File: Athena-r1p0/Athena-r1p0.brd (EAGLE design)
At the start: 33 x 55.1 mm, 81 parts, among them J1 MF-CON-MICROUSB-RIGHT, J2 G800LS588010THR, J3 TC2030-IDC-NL, J4 MF-CON-2.54mm-01x08, J5 MF-CON-2.54mm-01x08, J6 MF-CON-2.54mm-01x07, SW1 MF-SW-TACT-6MM, SW2 MF-SW-TACT-6MM, U1 PRTR5V0U2X,215, U2 MCP73831/2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

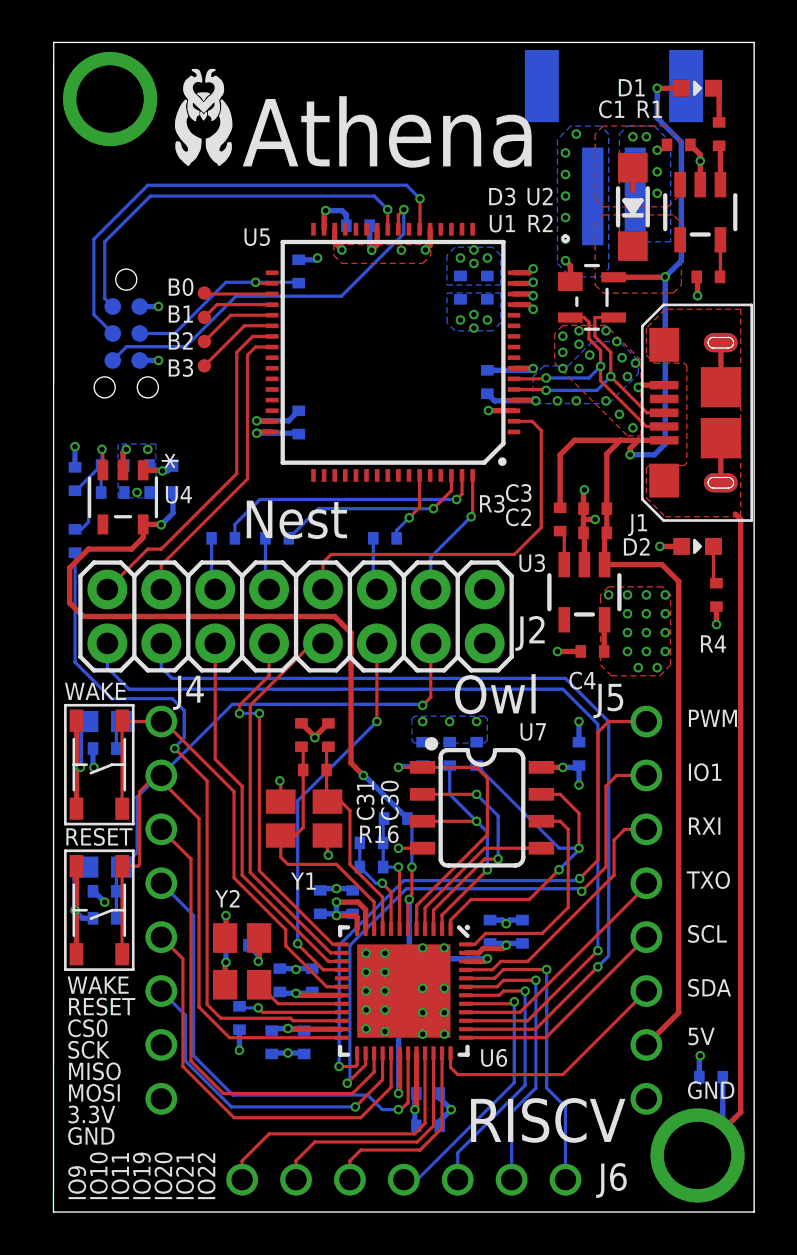
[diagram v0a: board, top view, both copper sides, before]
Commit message: Updated design
Removed off-board debug header
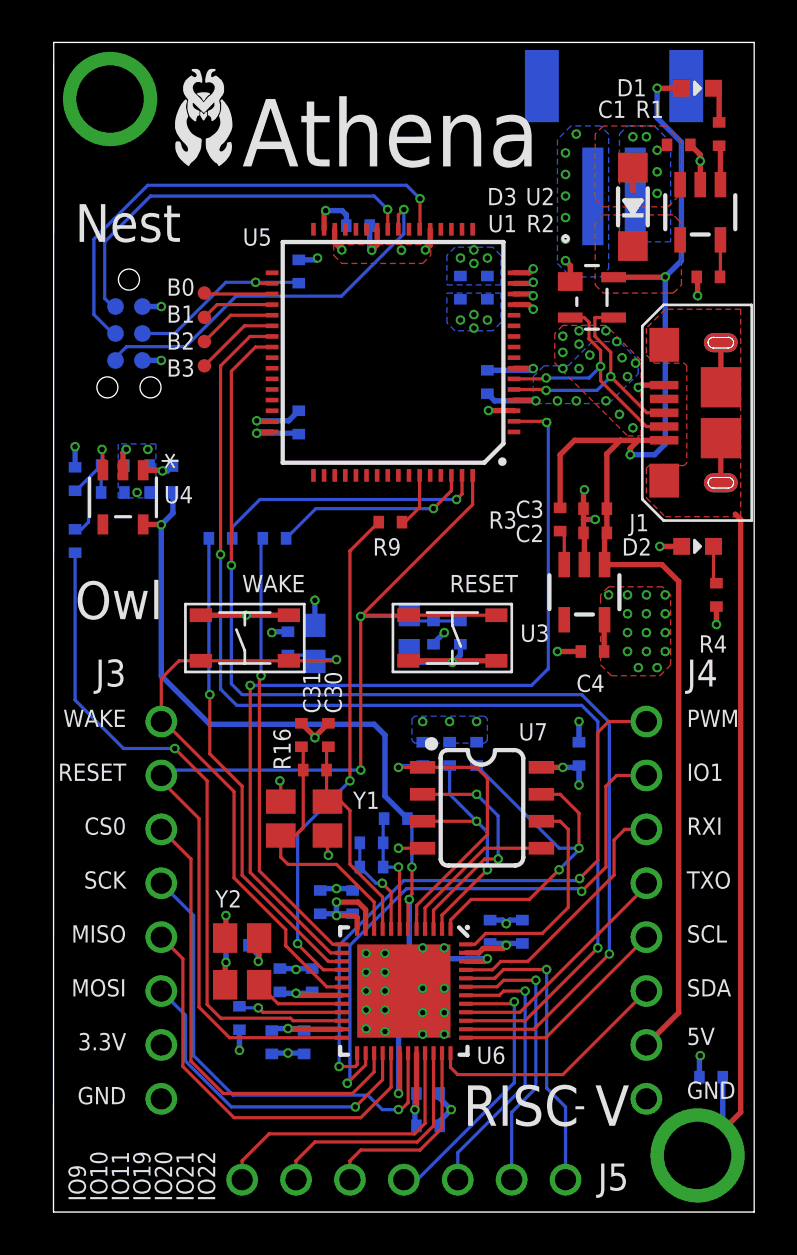
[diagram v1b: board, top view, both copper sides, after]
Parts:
- removed J6: MF-CON-2.54mm-01x07, Athena-r1p0:PTH_2.54MM_01X07
- J2: value G800LS588010THR -> TC2030-IDC-NL; device Athena-r1p0:2X8 -> Athena-r1p0:TAG_TC2030-IDC-NL
- J3: value TC2030-IDC-NL -> MF-CON-2.54mm-01x08; device Athena-r1p0:TAG_TC2030-IDC-NL -> Athena-r1p0:PTH_2.54MM_01X08
- J5: value MF-CON-2.54mm-01x08 -> MF-CON-2.54mm-01x07; device Athena-r1p0:PTH_2.54MM_01X08 -> Athena-r1p0:PTH_2.54MM_01X07
- moved J3 27.2 mm to (5.08, 14.2), flipped to the top
- moved J4 22.9 mm to (27.9, 14.2)
- moved C28 21.5 mm to (19.2, 27.3), turned to 270 degrees
- moved SW2 21.0 mm to (18.8, 27.1), turned to 180 degrees
- moved R14 19.7 mm to (17.9, 27.3), turned to 90 degrees
- moved D5 18.1 mm to (16.8, 27.3), turned to 90 degrees
- moved J5 17.1 mm to (16.5, 1.52), turned to 0 degrees
- moved J2 14.6 mm to (3.56, 41.4), flipped to the bottom, turned to 270 degrees
- moved D4 10.6 mm to (12.3, 26.8), turned to 270 degrees
- moved R13 9.96 mm to (11.0, 26.8), turned to 270 degrees
- moved SW1 9.09 mm to (9.02, 27.1), turned to 0 degrees
- moved R9 0.80 mm to (15.9, 32.5), flipped to the top, turned to 180 degrees
- moved R10 0.13 mm to (10.4, 31.8)
- moved R11 0.13 mm to (7.87, 31.8)
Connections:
- removed net JTAG_TCK_NEST: J2.8, R10.P$2
- removed net JTAG_TDI_NEST: J2.12, R9.P$2
- removed net JTAG_TDO_NEST: J2.10, U5.2
- removed net JTAG_TMS_NEST: J2.6, R11.P$1
- removed net RESET_NEST: J2.14, U5.64
- removed net UART_RX: J2.3, U6.38
- removed net UART_RX_NEST: J2.2, U5.39
- removed net UART_TX: J2.1, U6.39
- removed net UART_TX_NEST: J2.4, U5.40
- new net UART_RX_MK22: U5.39, U6.39
- new net UART_TX_MK22: U5.40, U6.38
- net 3.3V: now also J2.1, J3.P$7; no longer J3.1, J4.P$7
- net CS0: now also J3.P$3; no longer J4.P$3
- net DBG_RESET: now also J2.3; no longer J3.3
- net DBG_SWDCLK: now also J2.4; no longer J3.4
- net DBG_SWDIO: now also J2.2; no longer J3.2
- net DBG_SWO: now also J2.6; no longer J3.6
- net GND: now also J2.5, J3.P$8, MGT2.P$1; no longer J2.15, J2.16, J3.5, J5.P$8
- net IO1: now also J4.P$2; no longer J5.P$2
- net IO10: now also J5.P$2; no longer J6.P$2
- net IO11: now also J5.P$3; no longer J6.P$3
- net IO19: now also J5.P$4; no longer J6.P$4
- net IO20: now also J5.P$5; no longer J6.P$5
- net IO21: now also J5.P$6; no longer J6.P$6
- net IO22: now also J5.P$7; no longer J6.P$7
- net IO9: now also J5.P$1; no longer J6.P$1
- net JTAG_TCK: now also R10.P$2; no longer J2.7
- net JTAG_TDI: now also R9.P$2; no longer J2.11
- net JTAG_TDO: now also U5.2; no longer J2.9
- net JTAG_TMS: now also R11.P$1; no longer J2.5
- net MISO: now also J3.P$5; no longer J4.P$5
- net MOSI: now also J3.P$6; no longer J4.P$6
- net PWM: now also J4.P$1; no longer J5.P$1
- net RESET: now also J3.P$2, U5.64; no longer J2.13, J4.P$2
- net RXI: now also J4.P$3; no longer J5.P$3
- net SCK: now also J3.P$4; no longer J4.P$4
- net SCL: now also J4.P$5; no longer J5.P$5
- net SDA: now also J4.P$6; no longer J5.P$6
- net TXO: now also J4.P$4; no longer J5.P$4
- net V_USB: now also J4.P$7; no longer J5.P$7
- net WAKE: now also J3.P$1; no longer J4.P$1
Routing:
- net UART_RX_MK22: track 0.00 -> 55.0 mm, vias 0 -> 2
- net UART_TX_MK22: track 0.00 -> 54.8 mm, vias 0 -> 2
- net UART_TX: track 43.6 -> 0.00 mm, vias 1 -> 0
- net UART_RX: track 42.5 -> 0.00 mm, vias 1 -> 0
- net JTAG_TDO: track 18.4 -> 42.3 mm, vias 0 -> 2
- net JTAG_TDO_NEST: track 18.3 -> 0.00 mm
- net UART_RX_NEST: track 16.0 -> 0.00 mm
- net UART_TX_NEST: track 14.0 -> 0.00 mm
- net 1.8V: track 54.2 -> 47.3 mm, vias 6 -> 5
- net RESET_NEST: track 6.19 -> 0.00 mm, vias 1 -> 0
- net JTAG_TDI: track 18.3 -> 24.1 mm
- net JTAG_TMS: track 17.8 -> 22.9 mm, vias 0 -> 1
- net WAKE: track 25.7 -> 29.6 mm, vias 0 -> 1
- net JTAG_TCK: track 17.6 -> 21.1 mm, vias 2 -> 1
- net RESET: track 53.2 -> 55.8 mm, vias 1 -> 2
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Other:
- board text added: "-"
- board text added: "RISC"
- board text added: "V"
- board text removed: "C:/Users/jhell/Downloads/sign.bmp"
- board text removed: "J2 Pinout"
- board text removed: "RISCV"
- board text removed: "RST"
- board text removed: "RX"
- board text removed: "RiceU"
- board text removed: "TCK"
- board text removed: "TDI"
- board text removed: "TDO"
- board text removed: "TMS"
- board text removed: "TX"
